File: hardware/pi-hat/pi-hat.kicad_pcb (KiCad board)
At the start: 4 copper layers, 65 x 56 mm, 18 parts, among them J3 40HAT, J6 CONN_02X02, J9 CONN_01X02, Q1 DMG2305UX, Q2 DMMT5401, U2 CAT24C32

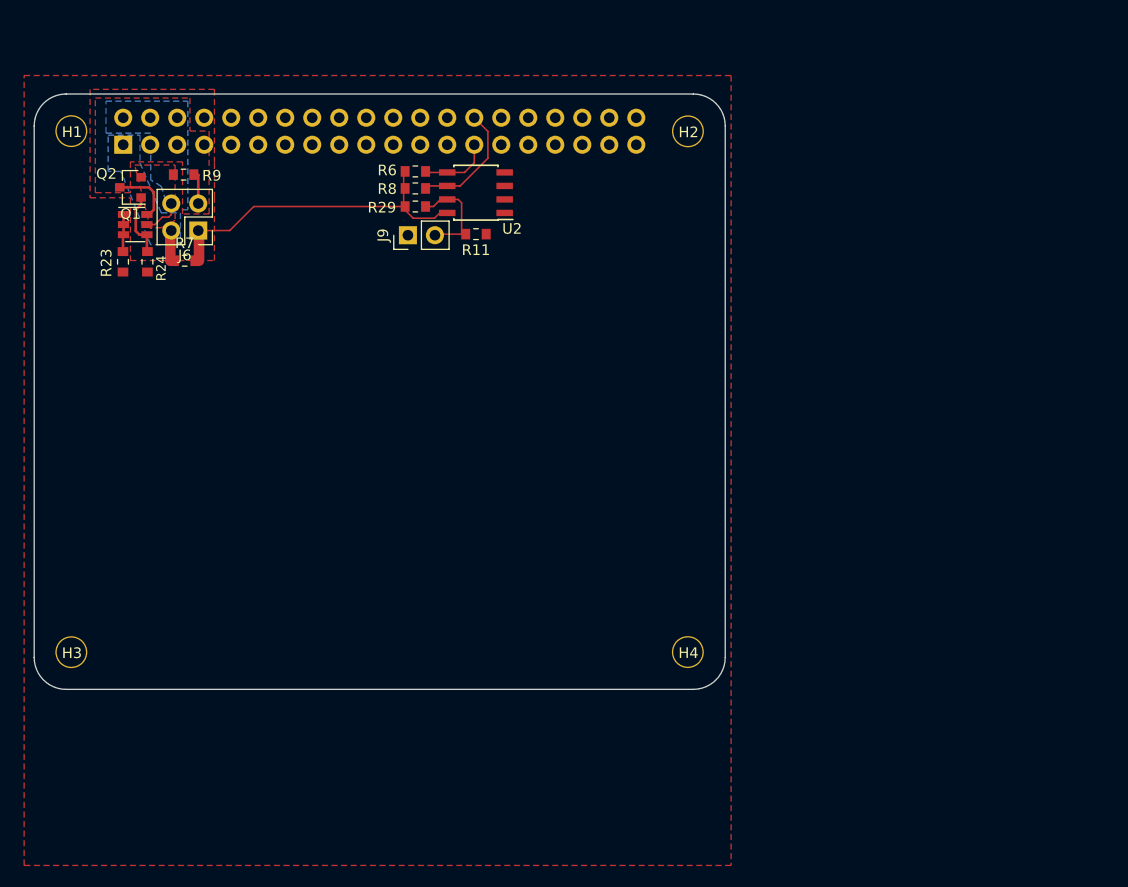
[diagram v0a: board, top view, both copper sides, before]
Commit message: footprint assignments and early board layout
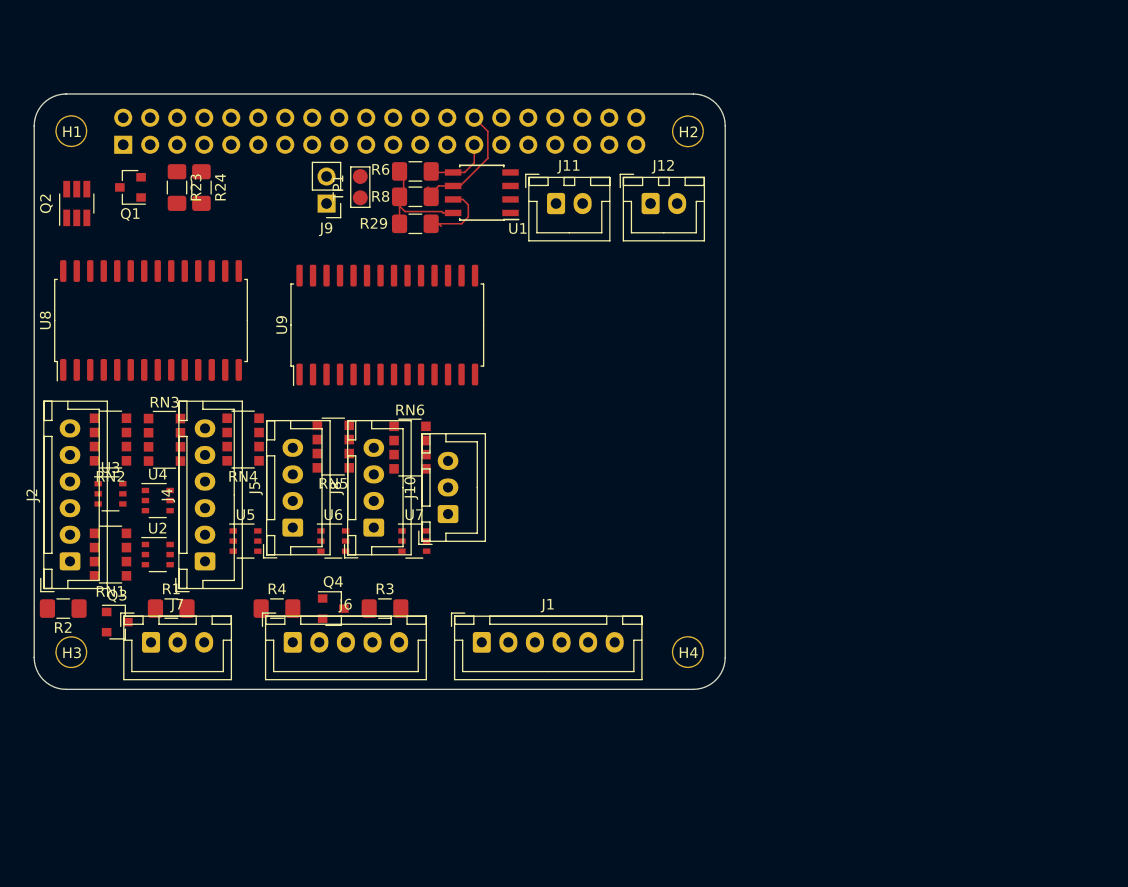
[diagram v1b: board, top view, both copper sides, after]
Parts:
- removed R11, R7, R9: DNP, Resistor_SMD:R_0603_1608Metric_Pad0.84x1.00mm_HandSolder
- added J1: PWR IN, Connector_JST:JST_XH_B6B-XH-A_1x06_P2.50mm_Vertical, F.Cu at (120.7, 112.4)
- added J10: 6-8, Connector_JST:JST_XH_B3B-XH-A_1x03_P2.50mm_Vertical, F.Cu at (117.5, 100.3)
- added J11: PWM0, Connector_JST:JST_XH_B2B-XH-A_1x02_P2.50mm_Vertical, F.Cu at (127.6, 71.1)
- added J12: PWM1, Connector_JST:JST_XH_B2B-XH-A_1x02_P2.50mm_Vertical, F.Cu at (136.5, 71.1)
- added J2: A-F, Connector_JST:JST_XH_B6B-XH-A_1x06_P2.50mm_Vertical, F.Cu at (81.9, 104.8)
- added J4: G-M, Connector_JST:JST_XH_B6B-XH-A_1x06_P2.50mm_Vertical, F.Cu at (94.6, 104.8)
- added J5: N-Q, Connector_JST:JST_XH_B4B-XH-A_1x04_P2.50mm_Vertical, F.Cu at (102.9, 101.6)
- added J7: PANEL_CTL, Connector_JST:JST_XH_B3B-XH-A_1x03_P2.50mm_Vertical, F.Cu at (89.5, 112.4)
- added J8: 2-5, Connector_JST:JST_XH_B4B-XH-A_1x04_P2.50mm_Vertical, F.Cu at (110.5, 101.6)
- added Q3: DMN6075S, Package_TO_SOT_SMD:SOT-23, F.Cu at (86.4, 110.5)
- added Q4: NTR4171P, Package_TO_SOT_SMD:SOT-23, F.Cu at (106.7, 109.2)
- added R1: 100R, Resistor_SMD:R_1206_3216Metric_Pad1.42x1.75mm_HandSolder, F.Cu at (91.4, 109.2)
- added R2: 10k, Resistor_SMD:R_1206_3216Metric_Pad1.42x1.75mm_HandSolder, F.Cu at (81.3, 109.2)
- added R3: 100R, Resistor_SMD:R_1206_3216Metric_Pad1.42x1.75mm_HandSolder, F.Cu at (111.5, 109.2)
- added R4: 10k, Resistor_SMD:R_1206_3216Metric_Pad1.42x1.75mm_HandSolder, F.Cu at (101.4, 109.2)
- added RN1: EXB-38V103JV, Resistor_SMD:R_Array_Convex_4x1206, F.Cu at (85.7, 104.1)
- added RN2: EXB-38V103JV, Resistor_SMD:R_Array_Convex_4x1206, F.Cu at (85.7, 93.3)
- added RN3: EXB-38V103JV, Resistor_SMD:R_Array_Convex_4x1206, F.Cu at (90.8, 93.3)
- added RN4: EXB-38V103JV, Resistor_SMD:R_Array_Convex_4x1206, F.Cu at (98.2, 93.3)
- added RN5: EXB-38V103JV, Resistor_SMD:R_Array_Convex_4x1206, F.Cu at (106.7, 94.0)
- added RN6: EXB-38V103JV, Resistor_SMD:R_Array_Convex_4x1206, F.Cu at (113.9, 94.1)
- added TP1: TP_WP, project_footprints:TestPoint_Bridge_Jumper_Pitch2.0mm, F.Cu at (109.2, 68.6)
- added U2: CM1293A, Package_SO:TSOP-6_1.65x3.05mm_P0.95mm, F.Cu at (90.2, 104.1)
- added U3: CM1293A, Package_SO:TSOP-6_1.65x3.05mm_P0.95mm, F.Cu at (85.7, 98.4)
- added U4: CM1293A, Package_SO:TSOP-6_1.65x3.05mm_P0.95mm, F.Cu at (90.2, 99.1)
- added U5: CM1293A, Package_SO:TSOP-6_1.65x3.05mm_P0.95mm, F.Cu at (98.4, 102.9)
- added U6: CM1293A, Package_SO:TSOP-6_1.65x3.05mm_P0.95mm, F.Cu at (106.7, 102.9)
- added U7: CM1293A, Package_SO:TSOP-6_1.65x3.05mm_P0.95mm, F.Cu at (114.3, 102.9)
- added U8: MCP23S17_SO, Package_SO:SOIC-28W_7.5x17.9mm_P1.27mm, F.Cu at (89.5, 82.1)
- added U9: MCP23S17_SO, Package_SO:SOIC-28W_7.5x17.9mm_P1.27mm, F.Cu at (111.8, 82.5)
- J6: value CONN_02X02 -> PANEL_PWR; footprint Connector_PinHeader_2.54mm:PinHeader_2x02_P2.54mm_Vertical -> Connector_JST:JST_XH_B5B-XH-A_1x05_P2.50mm_Vertical
- J9: value CONN_01X02 -> WP
- Q2: footprint Package_TO_SOT_SMD:SOT-23-6 -> Package_TO_SOT_SMD:SOT-23-6_Handsoldering
- R23, R24, R29, R6, R8: footprint Resistor_SMD:R_0603_1608Metric_Pad0.84x1.00mm_HandSolder -> Resistor_SMD:R_1206_3216Metric_Pad1.42x1.75mm_HandSolder
- moved J6 39.7 mm to (102.9, 112.4), turned to 0 degrees
- moved R23 8.64 mm to (92.0, 69.6)
- moved R24 8.64 mm to (94.3, 69.6)
- moved J9 8.21 mm to (106.0, 71.1), turned to 180 degrees
- moved Q2 5.85 mm to (82.5, 71.1), turned to 90 degrees
- moved R29 1.62 mm to (114.4, 73.0)
- moved R8 0.78 mm to (114.4, 70.5)
- moved U1 0.55 mm to (120.7, 70.1)
- renumbered U2 to U1
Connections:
- net Net-(J9-Pad2) renamed /WP
- J3 pad 16: (no net) -> /SPI_CS
- J3 pad 18: (no net) -> /IO_INT
- J3 pad 19: (no net) -> /SPI_MISO
- J3 pad 21: (no net) -> /SPI_MOSI
- J3 pad 23: (no net) -> /SPI_CLK
- J3 pad 32: (no net) -> /PWM0
- J3 pad 33: (no net) -> /PWM1
- J6 pad 1: /P3V3 -> /PANEL_30V
- J6 pad 2: /P3V3_HAT -> /PANEL_30V
- J6 pad 3: /P5V -> (no net)
- J6 pad 4: /P5V_HAT -> GND
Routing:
- net /P3V3: track 31.3 -> 10.3 mm
- net /P5V: track 8.71 -> 0.00 mm
- net Net-(Q1-Pad1): track 6.02 -> 0.07 mm
- net /P5V_HAT: track 3.77 -> 0.05 mm
- net Net-(Q2-Pad1): track 3.37 -> 0.00 mm
- net /P3V3_HAT: track 2.88 -> 0.00 mm
- net /WP: track 9.58 -> 7.60 mm
- net /ID_SC_EEPROM: track 11.7 -> 12.2 mm
- removed copper zone on B.Cu, net /P3V3_HAT
- removed copper zone on F.Cu, net /P5V
- removed copper zone on B.Cu, net /P5V_HAT
- removed copper zone on F.Cu, net /P5V_HAT
- removed copper zone on F.Cu, net GND

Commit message: first power traces
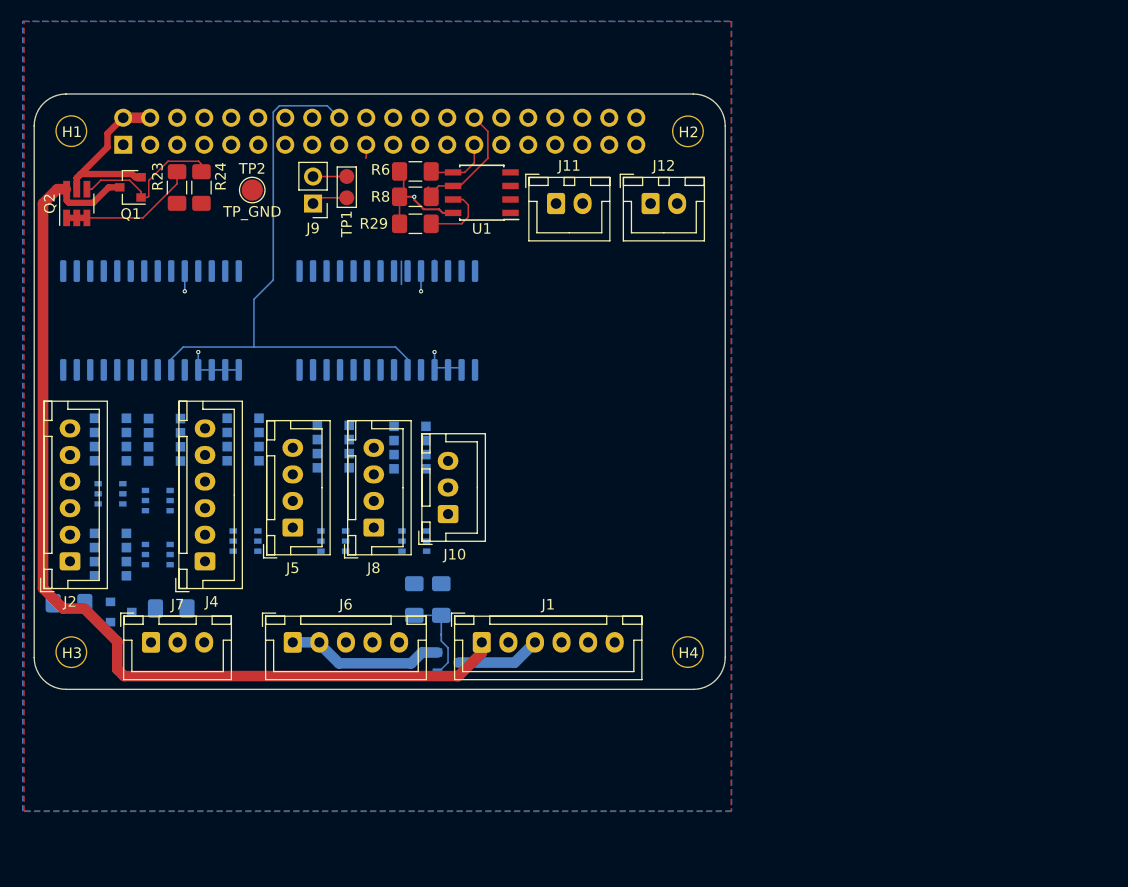
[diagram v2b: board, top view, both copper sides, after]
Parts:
- added TP2: TP_GND, TestPoint:TestPoint_Pad_D2.0mm, F.Cu at (99.1, 69.8)
- Q3, Q4, R1, R2, R3, R4, RN1, RN2, RN3, RN4, RN5, RN6, U2, U3, U4, U5, U6, U7, U8, U9: moved to B.Cu
- moved R4 12.9 mm to (114.3, 108.4), turned to 90 degrees
- moved Q4 11.9 mm to (117.5, 114.3)
- moved R3 5.37 mm to (116.8, 108.4), turned to 90 degrees
- moved J9 1.27 mm to (104.8, 71.1)
- moved TP1 1.27 mm to (108.0, 68.6)
- moved Q3 1.02 mm to (86.7, 109.5)
- moved R2 0.74 mm to (81.8, 108.7), turned to 0 degrees
- moved U9 0.43 mm to (111.8, 82.1), turned to 270 degrees
- turned U8 to 270 degrees
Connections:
- J3 pad 1: /P3V3_HAT -> /P3V3
- J3 pad 17: (no net) -> /P3V3
- U2 pad 5: /P3V3_HAT -> /P3V3
- U3 pad 5: /P3V3_HAT -> /P3V3
- U4 pad 5: /P3V3_HAT -> /P3V3
- U5 pad 5: /P3V3_HAT -> /P3V3
- U6 pad 5: /P3V3_HAT -> /P3V3
- U7 pad 5: /P3V3_HAT -> /P3V3
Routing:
- net /P5V: track 0.00 -> 93.8 mm
- net /IO_INT: track 0.00 -> 55.0 mm
- net /P5V_HAT: track 0.05 -> 17.4 mm
- net GND: track 0.00 -> 16.7 mm, vias 0 -> 4
- net Net-(Q1-Pad1): track 0.07 -> 15.3 mm
- net /PANEL_30V: track 0.00 -> 14.9 mm
- net Net-(Q2-Pad1): track 0.00 -> 12.8 mm
- net Net-(Q4-Pad1): track 0.00 -> 8.84 mm
- net /P30V: track 0.00 -> 7.96 mm
- net /SPI_MISO: track 0.00 -> 3.46 mm
- net /WP: track 7.60 -> 9.72 mm
- net /SPI_CS: track 0.00 -> 1.03 mm
- net /P3V3: track 10.3 -> 10.1 mm, vias 0 -> 1
- added copper zone on B.Cu, net /P3V3
- added copper zone on F.Cu, net GND
- removed copper zone on In2.Cu, net GND
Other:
- board text removed: "If you want to use an SMT 40-pin header, please move the top edge up by 0.5mm and locate the header in the same location as the current TH part."
- board text removed: "This is a HAT compatible PCB starting design based on the official Raspberry Pi specs at: https://github.com/raspberrypi/hats/blob/master/designguide.md Currently the camera slot and display cutout are not here. See the schematic for the details on the EEPROM and power setup. This board does have the correct components for powering the Pi via the HAT. If you need the Pi to provide 5V or 3.3V, ple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"

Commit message: add audio section with split gnd and 3v3
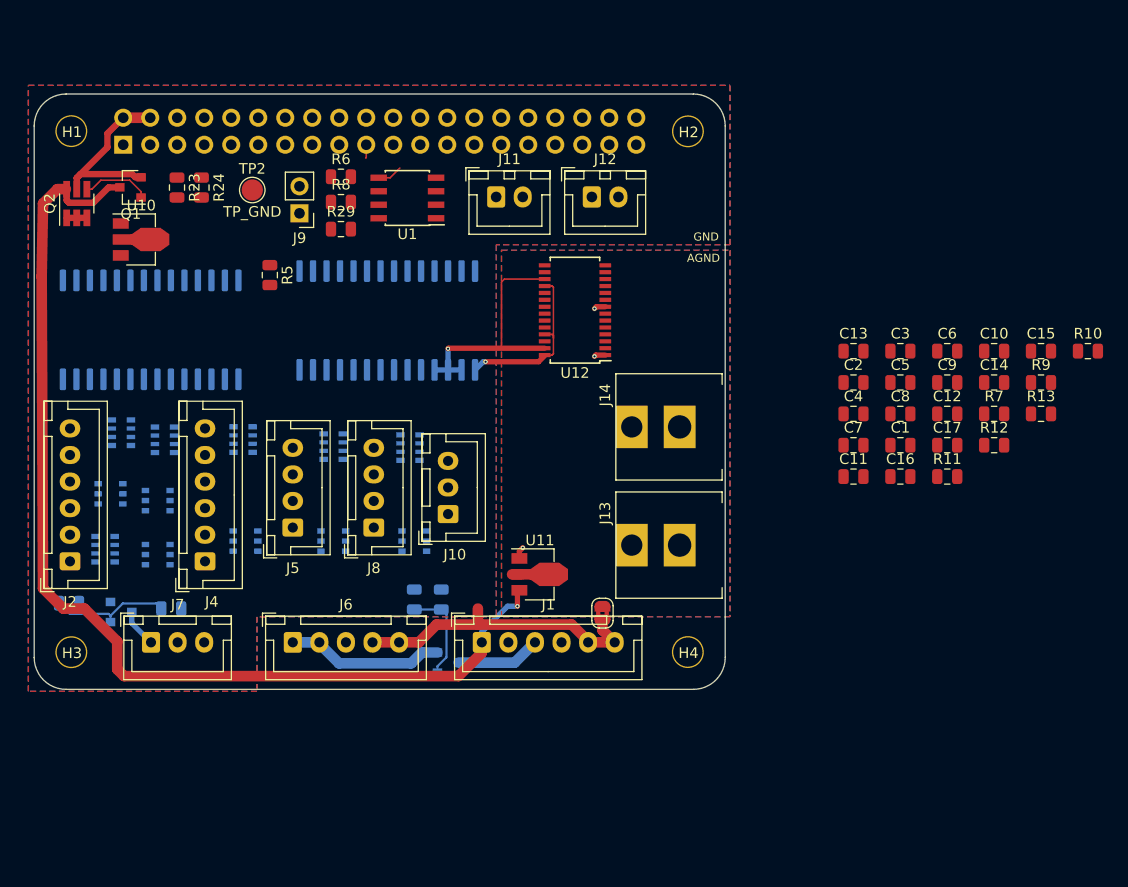
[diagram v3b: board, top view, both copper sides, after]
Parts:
- removed TP1: TP_WP, project_footprints:TestPoint_Bridge_Jumper_Pitch2.0mm
- added C1: 10uF, Capacitor_SMD:C_0805_2012Metric, F.Cu at (160.0, 93.9)
- added C10: 10uF, Capacitor_SMD:C_0805_2012Metric, F.Cu at (168.8, 85.0)
- added C11: 10uF, Capacitor_SMD:C_0805_2012Metric, F.Cu at (155.6, 96.8)
- added C12: .1uF, Capacitor_SMD:C_0805_2012Metric, F.Cu at (164.4, 90.9)
- added C13: 2.2uF, Capacitor_SMD:C_0805_2012Metric, F.Cu at (155.6, 85.0)
- added C14: 10uF, Capacitor_SMD:C_0805_2012Metric, F.Cu at (168.8, 88.0)
- added C15: .1uF, Capacitor_SMD:C_0805_2012Metric, F.Cu at (173.2, 85.0)
- added C16: 10uF, Capacitor_SMD:C_0805_2012Metric, F.Cu at (160.0, 96.8)
- added C17: .1uF, Capacitor_SMD:C_0805_2012Metric, F.Cu at (164.4, 93.9)
- added C2: .1uF, Capacitor_SMD:C_0805_2012Metric, F.Cu at (155.6, 88.0)
- added C3: 10uF, Capacitor_SMD:C_0805_2012Metric, F.Cu at (160.0, 85.0)
- added C4: .1uF, Capacitor_SMD:C_0805_2012Metric, F.Cu at (155.6, 90.9)
- added C5: 10uF, Capacitor_SMD:C_0805_2012Metric, F.Cu at (160.0, 88.0)
- added C6: .1uF, Capacitor_SMD:C_0805_2012Metric, F.Cu at (164.4, 85.0)
- added C7: 2.2uF, Capacitor_SMD:C_0805_2012Metric, F.Cu at (155.6, 93.9)
- added C8: 2.2uF, Capacitor_SMD:C_0805_2012Metric, F.Cu at (160.0, 90.9)
- added C9: 2.2uF, Capacitor_SMD:C_0805_2012Metric, F.Cu at (164.4, 88.0)
- added J13: KLPX-0848A-2-B, project_footprints:KLPX_RCA, F.Cu at (143.3, 103.3)
- added J14: KLPX-0848A-2-R, project_footprints:KLPX_RCA, F.Cu at (143.3, 92.1)
- added JP1: Jumper_NC_Small, Jumper:SolderJumper-2_P1.3mm_Bridged2Bar_RoundedPad1.0x1.5mm, F.Cu at (132.0, 109.7)
- added R10: 3.9K, Resistor_SMD:R_0805_2012Metric, F.Cu at (177.7, 85.0)
- added R11: 3.9K, Resistor_SMD:R_0805_2012Metric, F.Cu at (164.4, 96.8)
- added R12: 100R, Resistor_SMD:R_0805_2012Metric, F.Cu at (168.8, 93.9)
- added R13: 100R, Resistor_SMD:R_0805_2012Metric, F.Cu at (173.2, 90.9)
- added R5: 10k, Resistor_SMD:R_0805_2012Metric, F.Cu at (100.7, 77.9)
- added R7: 470R, Resistor_SMD:R_0805_2012Metric, F.Cu at (168.8, 90.9)
- added R9: 470R, Resistor_SMD:R_0805_2012Metric, F.Cu at (173.2, 88.0)
- added U10: L78L33_SOT89, Package_TO_SOT_SMD:SOT-89-3, F.Cu at (88.2, 74.5)
- added U11: L78L33_SOT89, Package_TO_SOT_SMD:SOT-89-3, F.Cu at (125.7, 106.0)
- added U12: PCM5122PW, Package_SO:TSSOP-28_4.4x9.7mm_P0.65mm, F.Cu at (129.4, 81.2)
- R1, R2, R23, R24, R29, R3, R4, R6, R8: footprint Resistor_SMD:R_1206_3216Metric_Pad1.42x1.75mm_HandSolder -> Resistor_SMD:R_0805_2012Metric
- RN1, RN2, RN3, RN4, RN5, RN6: footprint Resistor_SMD:R_Array_Convex_4x1206 -> Resistor_SMD:R_Array_Convex_4x0603
- moved R29 7.02 mm to (107.4, 73.5)
- moved R6 7.02 mm to (107.4, 68.6)
- moved R8 7.02 mm to (107.4, 71.0)
- moved U1 7.02 mm to (113.7, 70.6)
- moved J11 5.67 mm to (122.0, 70.5)
- moved J12 5.56 mm to (131.0, 70.5)
- moved J9 1.57 mm to (103.5, 72.0)
- moved RN2 1.21 mm to (86.7, 92.7)
- moved U8 0.88 mm to (89.5, 83.0)
- moved RN1 0.72 mm to (85.2, 103.6), turned to 0 degrees
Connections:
- net /ID_SC_EEPROM renamed /ID_SCL
- net /ID_SD_EEPROM renamed /ID_SDA
- J3 pad 1: /P3V3 -> (no net)
- J3 pad 12: (no net) -> /PCM_CLK
- J3 pad 16: /SPI_CS -> (no net)
- J3 pad 17: /P3V3 -> (no net)
- J3 pad 18: /IO_INT -> /IO_INT_A
- J3 pad 22: (no net) -> /IO_INT_B
- J3 pad 24: (no net) -> /SPI_CS
- J3 pad 3: (no net) -> /I2C_SDA
- J3 pad 35: (no net) -> /PCM_FS
- J3 pad 40: (no net) -> /PCM_DATA
- J3 pad 5: (no net) -> /I2C_SCL
- U8 pad 20: /IO_INT -> /IO_INT_A
- U9 pad 20: /IO_INT -> /IO_INT_B
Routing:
- net /IO_INT: track 55.0 -> 0.00 mm
- net GND: track 16.7 -> 52.4 mm, vias 4 -> 1
- net Net-(Q3-Pad1): track 0.00 -> 11.4 mm
- net Net-(Q2-Pad1): track 12.8 -> 1.90 mm
- net /ID_SCL: track 12.2 -> 1.30 mm
- net /WP: track 9.72 -> 0.00 mm
- net Net-(Q1-Pad1): track 15.3 -> 6.52 mm
- net /P5V: track 93.8 -> 100.7 mm, vias 0 -> 1
- net /P3V3: track 10.1 -> 16.2 mm
- net /ID_SDA: track 7.43 -> 3.66 mm
- net /SOLENOID: track 0.00 -> 3.60 mm
- net /P3V3A: track 0.00 -> 3.28 mm, vias 0 -> 3
- net /SPI_MISO: track 3.46 -> 1.28 mm
- net /SPI_CS: track 1.03 -> 0.00 mm
- net GNDA: track 0.00 -> 0.83 mm
- added copper zone on B.Cu, net /P3V3A
- added copper zone on F.Cu, net GNDA
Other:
- board text added: "AGND"
- board text added: "GND"

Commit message: route io protection
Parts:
- moved U7 8.36 mm to (118.2, 95.5)
- moved U5 8.31 mm to (102.2, 95.5)
- moved U6 8.08 mm to (110.0, 95.5)
- moved RN4 7.63 mm to (102.2, 99.8), turned to 0 degrees
- moved RN6 7.15 mm to (118.2, 99.8)
- moved RN3 6.96 mm to (93.7, 99.7)
- moved RN5 6.75 mm to (110.1, 99.8), turned to 0 degrees
- moved U2 5.88 mm to (86.0, 100.0)
- moved U3 5.74 mm to (86.2, 92.7)
- moved U4 4.61 mm to (93.7, 96.0)
- moved J5 4.52 mm to (98.5, 102.8)
- moved J8 4.15 mm to (106.5, 102.8)
- moved J4 4.11 mm to (90.5, 104.8)
- moved RN2 3.58 mm to (86.1, 96.2), turned to 0 degrees
- moved J10 3.05 mm to (114.5, 101.0)
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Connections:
- J3 pad 17: (no net) -> /P3V3_HAT
- R29 pad 1: /P3V3 -> /P3V3_HAT
- R6 pad 1: /P3V3 -> /P3V3_HAT
- R8 pad 1: /P3V3 -> /P3V3_HAT
- RN2 pad 1: /E_IN -> /F_IN
- RN2 pad 2: /F_IN -> /E_IN
- U1 pad 8: /P3V3 -> /P3V3_HAT
- U3 pad 1: /H_IN -> /E_IN
- U3 pad 3: /G_IN -> /F_IN
- U3 pad 4: /F_IN -> /H_IN
- U3 pad 6: /E_IN -> /G_IN
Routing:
- net /IO_INT_A: track 0.00 -> 41.1 mm, vias 0 -> 1
- net /ANY_KEY_IN: track 0.00 -> 39.2 mm, vias 0 -> 2
- net /A: track 0.00 -> 30.0 mm, vias 0 -> 2
- net /M: track 0.00 -> 29.2 mm, vias 0 -> 2
- net GND: track 52.4 -> 81.5 mm, vias 1 -> 11
- net /B: track 0.00 -> 29.1 mm, vias 0 -> 2
- net /C: track 0.00 -> 27.9 mm, vias 0 -> 2
- net /L: track 0.00 -> 27.7 mm, vias 0 -> 2
- net /K: track 0.00 -> 26.6 mm, vias 0 -> 2
- net /D: track 0.00 -> 26.6 mm, vias 0 -> 2
- net /J: track 0.00 -> 24.3 mm, vias 0 -> 2
- net /H: track 0.00 -> 21.2 mm, vias 0 -> 2
- net /G: track 0.00 -> 20.4 mm, vias 0 -> 2
- net /E: track 0.00 -> 20.4 mm, vias 0 -> 2
- net /F: track 0.00 -> 20.1 mm, vias 0 -> 2
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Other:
- board text added: "30V"
